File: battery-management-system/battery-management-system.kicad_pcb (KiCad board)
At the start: 4 copper layers, 130 x 100 mm, 199 parts, among them J1 CELL4_PLUS, J10 VBAT+_CHARGE, J11 I2C, J12 MCU_SUPPLY, J13 LEDS, J14 -5V, J15 TEMP_CELL1, J16 TEMP_CELL2, J17 TEMP_CELL3, J18 TEMP_CELL4, J19 CHARGE/DISCHARGE, J2 CELL4_MINUS, J20 UART_INTERCONNECT, J21 UART_USB, J22 BALANCE_INPUTS, J23 BALANCE_CURRENT, J24 3V3, J25 5V, J26 18V, J27 BALANCE_CONTROL, J28 9V4, J3 CELL3_MINUS, J4 CELL2_MINUS, J5 CELL1_MINUS, J6 VBAT+, J7 AMPHENOL_micro_usb_10118194-0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, J8 VBAT-, J9 rspro_header_5pin_3_5mm, Q1 DMN3730U, Q10 DMN3730U, Q11 DMN3404L, Q12 DMN3730U, Q14 DMN3730U, Q15 DMN3730U, Q16 DMN3730U, Q17 DMN3730U, Q2 TJ40S04M3L, Q3 TJ40S04M3L, Q4 DMN3730U, Q5 DMN3730U, Q6 BS250FTA, Q7 BS250FTA, Q8 BS250FTA, Q9 BS250FTA, SW1 CELL1_MINUS, SW2 CELL1_PLUS, SW3 CELL2_MINUS, SW4 CELL2_PLUS, SW5 CELL3_PLUS, SW6 CELL3_MINUS, SW7 CELL4_PLUS, SW8 CELL4_MINUS, U1 L6982C33DR, U10 LM2904M8-13, U11 LM2904M8-13, U12 ICL7660, U13 MC74VHC139, U14 STC3100, U15 ICL7660, U16 ICL7660, U2 L6982C33DR, U3 FT230XS, U4 STM32L071CZTx, U5 ARM-JTAG-SWD, U6 LM2904M8-13, U7 LM2904M8-13, U8 AT24C512C, U9 NCT75DR2G

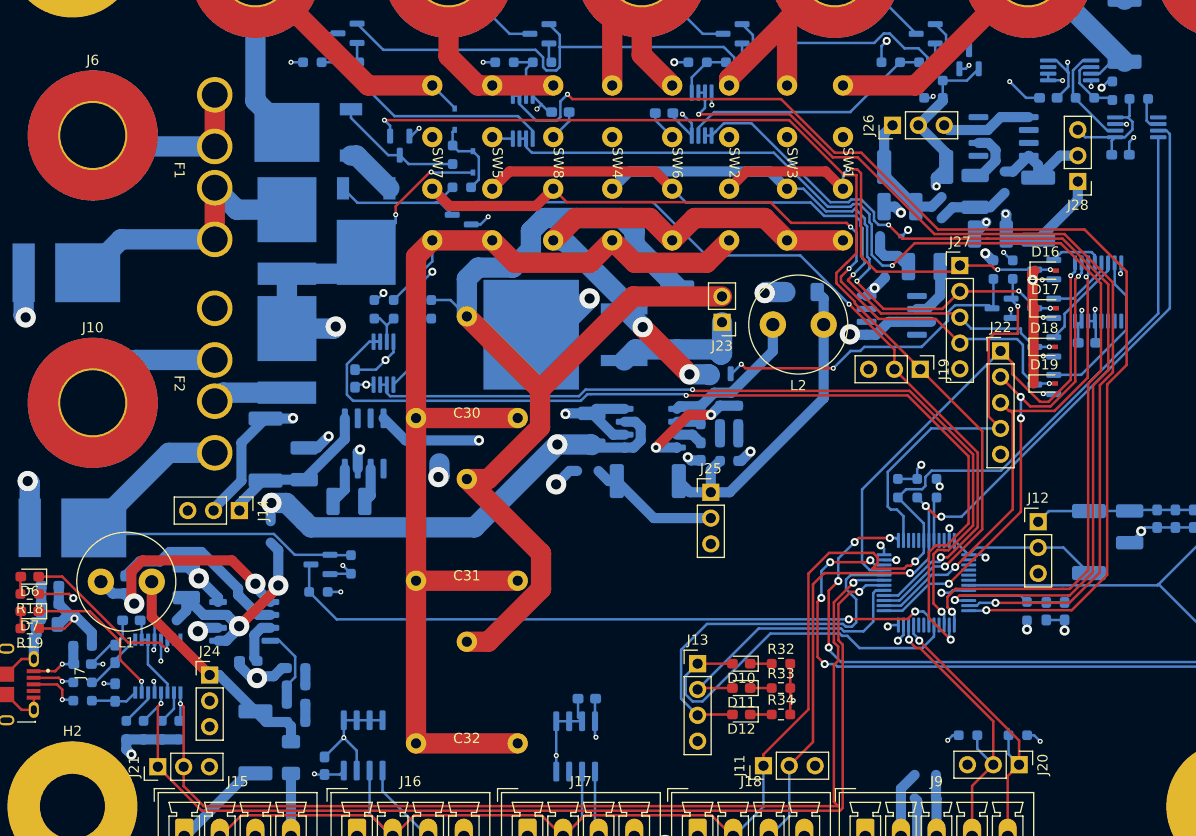
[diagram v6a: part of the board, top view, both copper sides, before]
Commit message: fix design rule errors
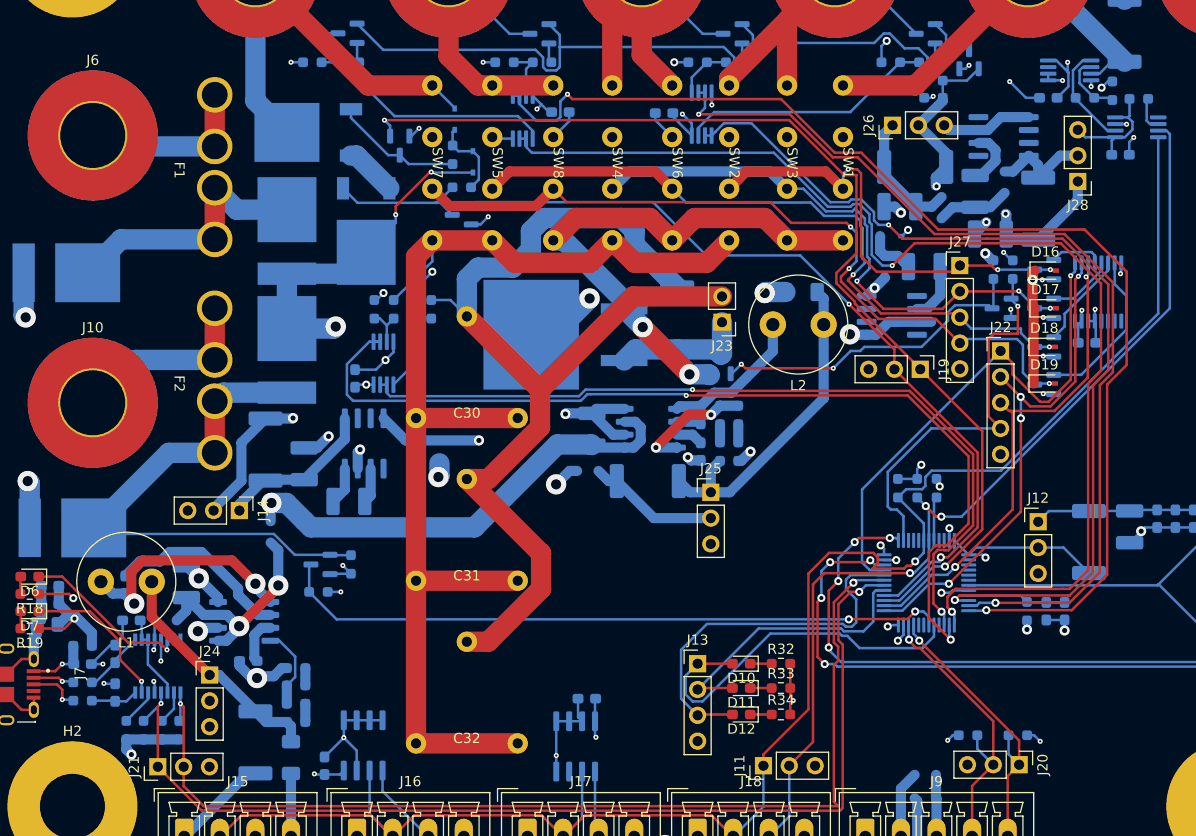
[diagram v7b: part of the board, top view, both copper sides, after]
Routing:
- net /5V_USB: track 164.6 -> 74.0 mm
- net Net-(J10-Pin_1): track 13.7 -> 18.8 mm
- net Net-(D14-K): track 48.8 -> 53.9 mm
- net /Interconnect/UART_TX: track 29.5 -> 28.9 mm
- net /PACK_EXT: vias 5 -> 4

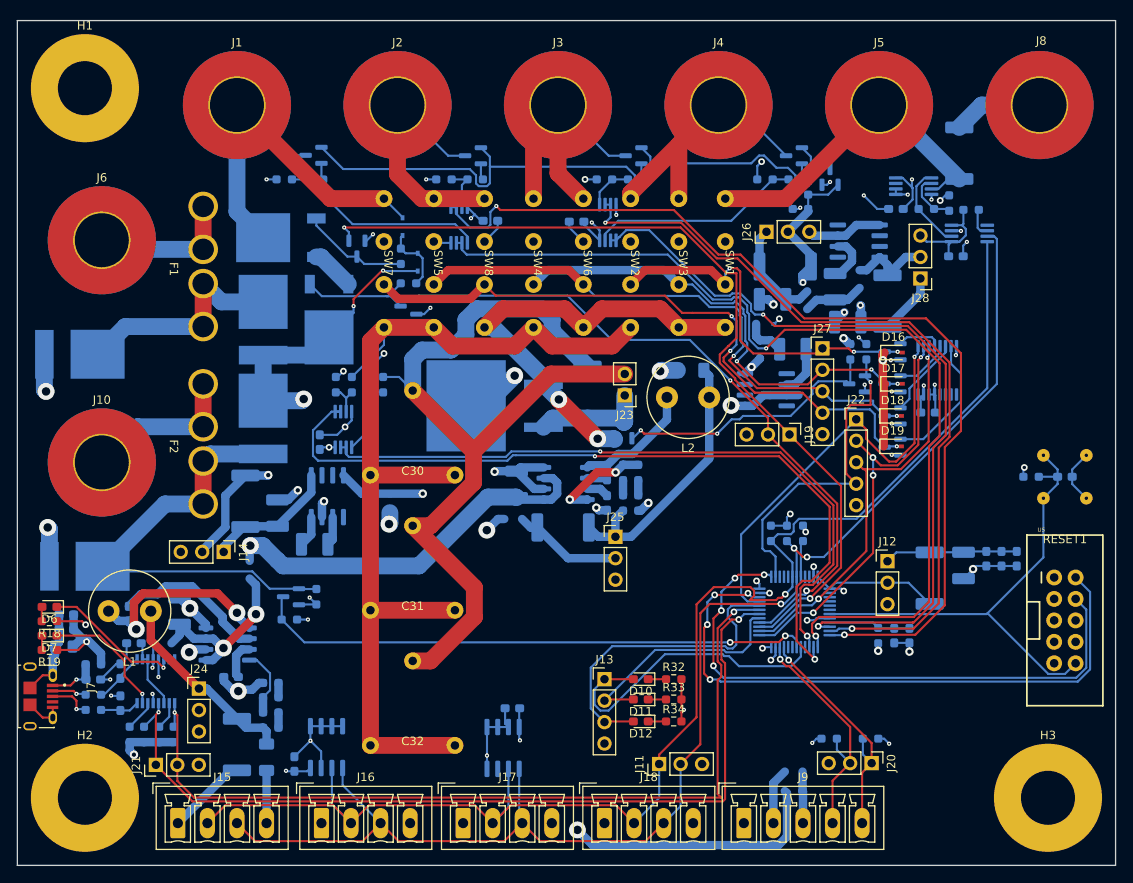
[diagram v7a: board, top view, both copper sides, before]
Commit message: fix design rule errors
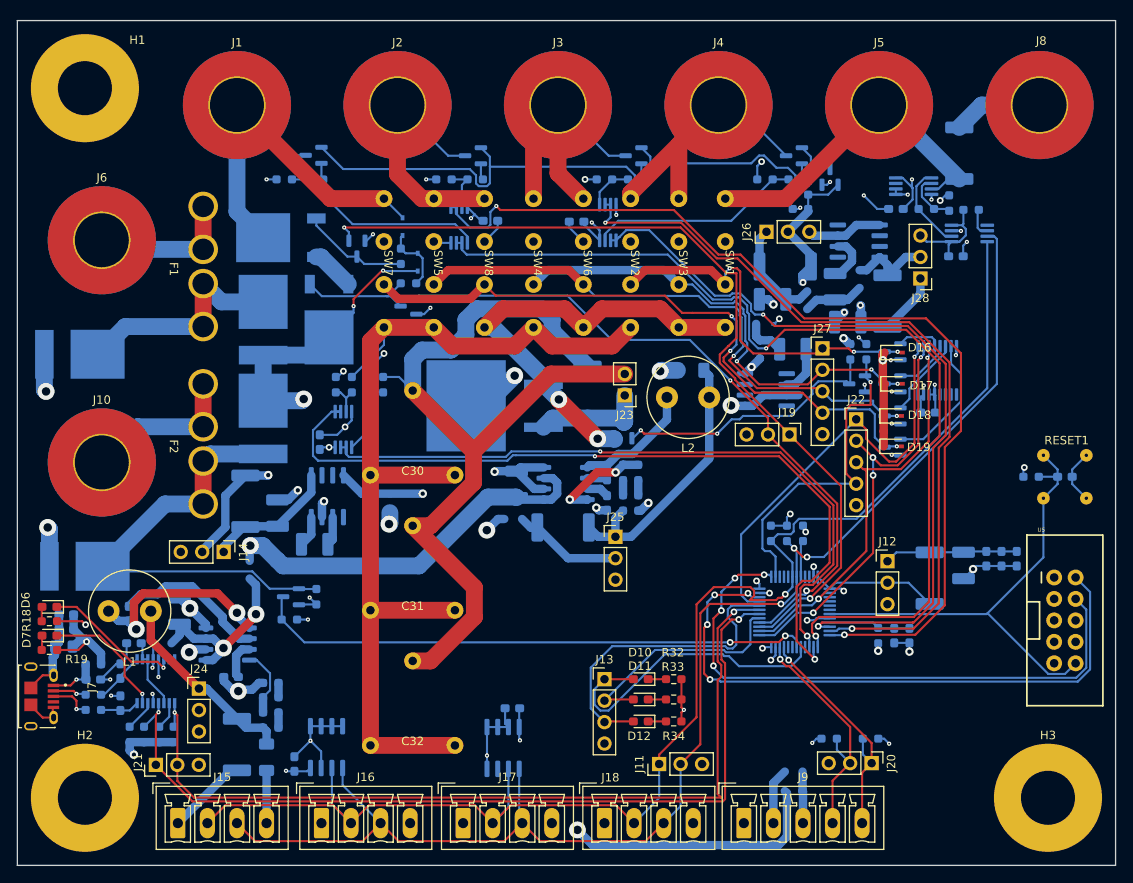
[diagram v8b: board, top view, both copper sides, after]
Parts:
- moved J7 0.10 mm to (21.6, 100.0)
